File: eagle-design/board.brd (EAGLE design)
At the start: 160 x 100 mm, 21 parts, among them IC1 7805T

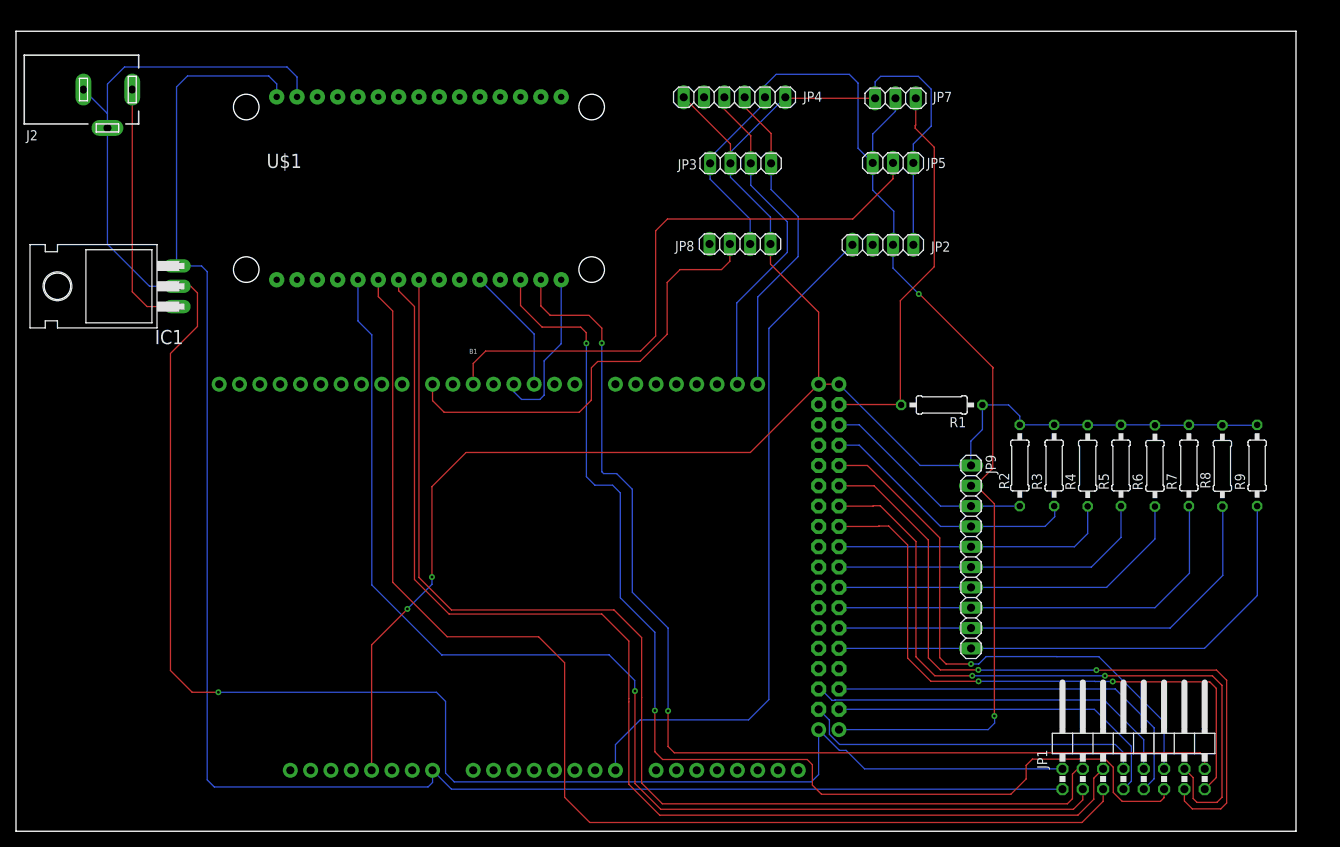
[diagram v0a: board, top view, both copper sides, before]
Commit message: Added motherboard design and image exports
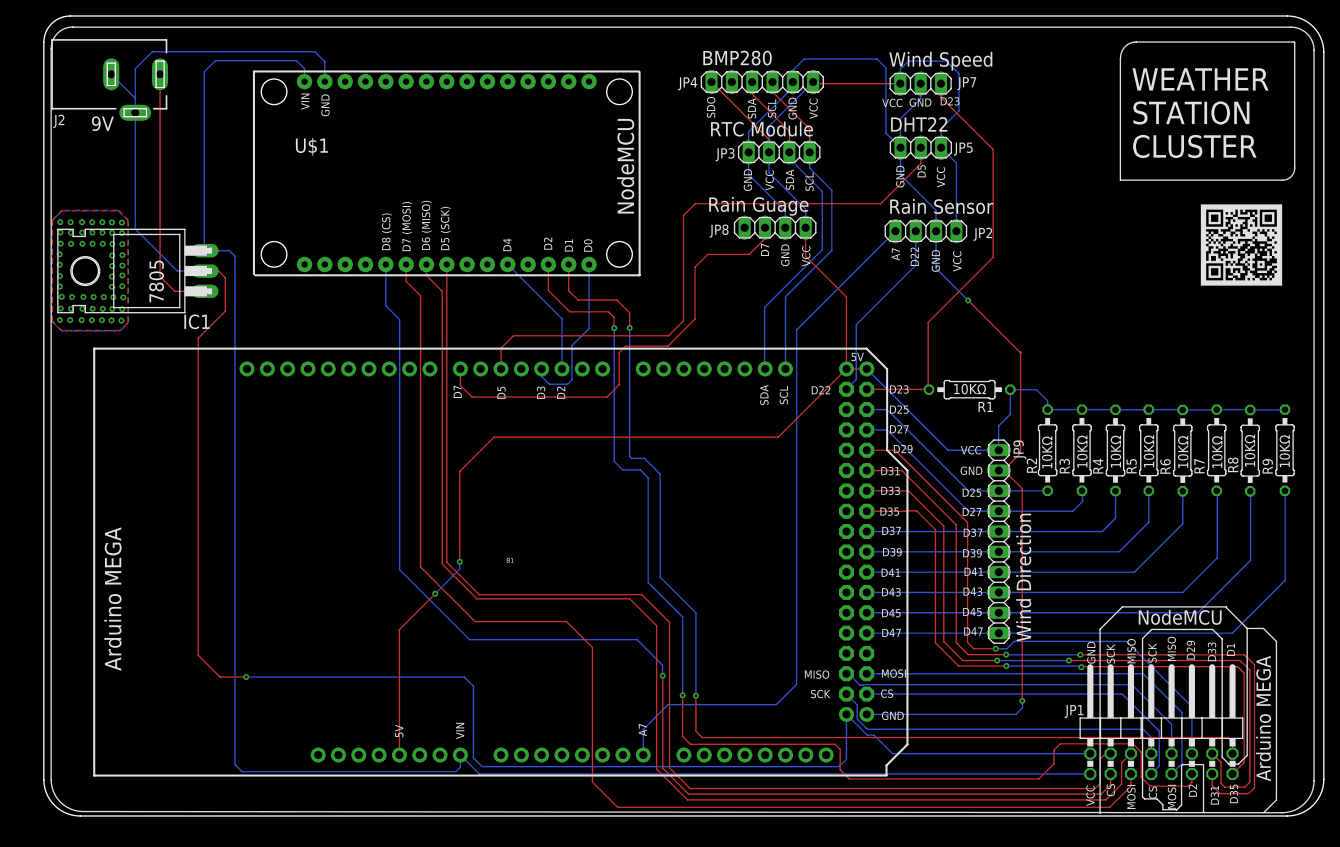
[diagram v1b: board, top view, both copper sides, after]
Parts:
- moved JP2 5.65 mm to (113.7, 75.0)
- moved JP3 5.02 mm to (95.4, 84.9)
- moved JP8 4.84 mm to (94.9, 75.4)
- moved JP1 3.97 mm to (143.2, 13.5)
- moved JP9 3.97 mm to (122.9, 36.2)
- moved R1 3.97 mm to (119.2, 55.2)
- moved R2 3.97 mm to (129.0, 47.6)
- moved R3 3.97 mm to (133.2, 47.6)
- moved R4 3.97 mm to (137.4, 47.6)
- moved R6 3.97 mm to (145.8, 47.6)
- moved R7 3.97 mm to (150.1, 47.6)
- moved J2 3.97 mm to (14.9, 94.6)
- moved IC1 3.97 mm to (13.5, 70.0)
- moved B1 3.97 mm to (59.4, 33.7)
- moved JP4 3.97 mm to (93.3, 93.6)
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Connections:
- new net N$36: B1.22, JP2.3
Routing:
- net N$36: track 0.00 -> 23.3 mm
- net N$5: track 48.9 -> 52.2 mm
- net N$7: track 156.7 -> 155.6 mm
- net N$3: track 255.4 -> 256.3 mm
- net N$11: track 41.8 -> 42.5 mm
- net N$6: track 40.7 -> 41.3 mm
- net N$8: track 85.9 -> 86.5 mm
- net N$12: track 56.0 -> 56.5 mm
- added copper zone on layer 1, net GND
- added copper zone on layer 16, net GND
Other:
- outline, holes or cut-outs redrawn
- board text added: "10KΩ"
- board text added: "5V"
- board text added: "7805"
- board text added: "9V"
- board text added: "A7"
- board text added: "Arduino MEGA"
- board text added: "BMP280"
- board text added: "CS"
- board text added: "D0"
- board text added: "D1"
- board text added: "D2"
- board text added: "D22"
- board text added: "D23"
- board text added: "D25"
- board text added: "D27"
- board text added: "D29"
- board text added: "D3"
- board text added: "D31"
- board text added: "D33"
- board text added: "D35"
- board text added: "D37"
- board text added: "D39"
- board text added: "D4"
- board text added: "D41"
- board text added: "D43"
- board text added: "D45"
- board text added: "D47"
- board text added: "D5"
- board text added: "D5 (SCK)"
- board text added: "D6 (MISO)"
- board text added: "D7"
- board text added: "D7 (MOSI)"
- board text added: "D8 (CS)"
- board text added: "DHT22"
- board text added: "GND"
- board text added: "MISO"
- board text added: "MOSI"
- board text added: "NodeMCU"
- board text added: "RTC Module"
- board text added: "Rain Guage"
- board text added: "Rain Sensor"
- board text added: "SCK"
- board text added: "SCL"
- board text added: "SDA"
- board text added: "SDO"
- board text added: "VCC"
- board text added: "VIN"
- board text added: "WEATHER STATION CLUSTER"
- board text added: "Wind Direction"
- board text added: "Wind Speed"
- board text added: "sashwat.in"

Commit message: Added new design
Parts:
- added R10, R11: 10k, rcl:0207/10
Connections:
- removed net N$11: B1.20, JP3.2, JP4.4
- removed net N$6: B1.21, JP3.1, JP4.3
- new net N$91: B1.21, JP3.1, JP4.3, R10.1
- new net N$92: B1.20, JP3.2, JP4.4, R11.1
- net N$3: now also R10.2, R11.2
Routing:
- net N$92: track 0.00 -> 99.5 mm, vias 0 -> 3
- net N$91: track 0.00 -> 90.6 mm, vias 0 -> 3
- net N$11: track 42.5 -> 0.00 mm
- net N$6: track 41.3 -> 0.00 mm
- net N$3: track 256.3 -> 283.5 mm

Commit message: Updated eagle design
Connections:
- net N$14: now also U$1.D3; no longer U$1.D0
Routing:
- net N$14: track 20.7 -> 13.8 mm
- net N$9: track 15.9 -> 20.6 mm, vias 0 -> 2
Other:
- board text removed: "D0"
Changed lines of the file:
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@@
 <text x="67.0306" y="72.5678" size="1.016" layer="21" rot="R90">D2</text>
 <text x="69.6214" y="72.3392" size="1.016" layer="21" rot="R90">D1</text>
-<text x="72.0344" y="72.3138" size="1.016" layer="21" rot="R90">D0</text>
+<text x="64.4144" y="72.517" size="1.016" layer="21" rot="R90">D3</text>
 <text x="36.6776" y="90.17" size="1.016" layer="21" rot="R90">VIN</text>
 <text x="39.1922" y="89.3064" size="1.016" layer="21" rot="R90">GND</text>
@@
 <contactref element="B1" pad="2"/>
 <contactref element="U$1" pad="D4"/>
-<wire x1="61.468" y1="70.8406" x2="68.2498" y2="64.058871875" width="0.1524" layer="16"/>
-<wire x1="68.2498" y1="64.058871875" x2="68.2498" y2="57.785" width="0.1524" layer="16"/>
+<wire x1="61.468" y1="70.8406" x2="61.468" y2="65.9384" width="0.1524" layer="16"/>
+<via x="68.2244" y="64.1096" extent="1-16" drill="0.35"/>
+<wire x1="69.723" y1="63.6778" x2="69.2912" y2="64.1096" width="0.1524" layer="16"/>
+<wire x1="69.2912" y1="64.1096" x2="68.2244" y2="64.1096" width="0.1524" layer="16"/>
+<wire x1="69.723" y1="63.6778" x2="69.723" y2="59.2582" width="0.1524" layer="16"/>
+<wire x1="68.2498" y1="57.785" x2="69.723" y2="59.2582" width="0.1524" layer="16"/>
+<via x="64.1604" y="64.1096" extent="1-16" drill="0.35"/>
+<wire x1="64.1604" y1="64.1096" x2="63.2968" y2="64.1096" width="0.1524" layer="16"/>
+<wire x1="61.468" y1="65.9384" x2="63.2968" y2="64.1096" width="0.1524" layer="16"/>
+<wire x1="64.1604" y1="64.1096" x2="68.2244" y2="64.1096" width="0.1524" layer="1"/>
 </signal>
 <signal name="N$14">
-<contactref element="U$1" pad="D0"/>
 <contactref element="B1" pad="3"/>
-<wire x1="71.628" y1="70.8406" x2="71.628" y2="62.8396" width="0.1524" layer="16"/>
-<wire x1="69.4944" y1="60.706" x2="69.4944" y2="56.4134" width="0.1524" layer="16"/>
-<wire x1="69.4944" y1="56.4134" x2="68.961" y2="55.88" width="0.1524" layer="16"/>
-<wire x1="68.961" y1="55.88" x2="66.675" y2="55.88" width="0.1524" layer="16"/>
-<wire x1="66.675" y1="55.88" x2="65.7098" y2="56.8452" width="0.1524" layer="16"/>
-<wire x1="65.7098" y1="56.8452" x2="65.7098" y2="57.785" width="0.1524" layer="16"/>
-<wire x1="71.628" y1="62.8396" x2="69.4944" y2="60.706" width="0.1524" layer="16"/>
+<contactref element="U$1" pad="D3"/>
+<wire x1="64.008" y1="70.8406" x2="64.008" y2="67.6656" width="0.1524" layer="16"/>
+<wire x1="64.008" y1="67.6656" x2="65.7352" y2="65.9384" width="0.1524" layer="16"/>
+<wire x1="65.7352" y1="65.9384" x2="65.7352" y2="57.8104" width="0.1524" layer="16"/>
+<wire x1="65.7352" y1="57.8104" x2="65.7098" y2="57.785" width="0.1524" layer="16"/>
 </signal>
 <signal name="N$15">
